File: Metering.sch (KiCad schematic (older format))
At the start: 18 parts, among them J1 Barrel_Jack_Switch, J10 Conn_01x15, J11 Conn_01x11, J2 Conn_01x15_Female, J3 Conn_01x15_Female, J4 Conn_01x15_Female, J5 Conn_01x15_Female, J6 Conn_01x15_Female, J7 Conn_01x15_Female, J8 Conn_01x15_Female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

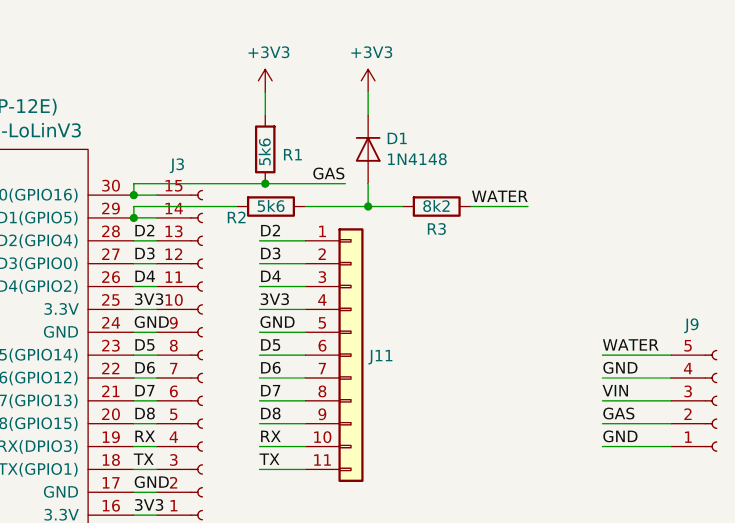
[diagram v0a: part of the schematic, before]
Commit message: add drills
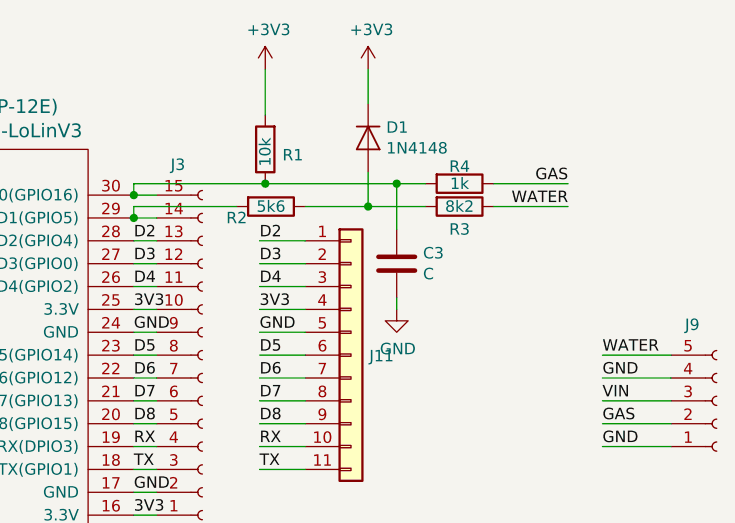
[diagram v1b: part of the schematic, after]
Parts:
- added C3: C, Capacitor_THT:C_Disc_D3.0mm_W2.0mm_P2.50mm, symbol Device:C
- added R4: 1k, w_pth_resistors:RC03, symbol Device:R
- R1: value 5k6 -> 10k
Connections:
- net GAS: now also R4.1; no longer J3.15 (Pin_15), R1.1, U1.30 (D0(GPIO16))
- net GND: now also C3.2
- new net: C3.1, J3.15 (Pin_15), R1.1, R4.2, U1.30 (D0(GPIO16))
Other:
- moved on the sheet: D1, R3
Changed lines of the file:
@@
 P 6875 3000
 F 0 "R1" H 6800 3025 50  0000 R CNN
-F 1 "5k6" V 6875 3075 50  0000 R CNN
+F 1 "10k" V 6875 3075 50  0000 R CNN
 F 2 "w_pth_resistors:RC03" V 6805 3000 50  0001 C CNN
 F 3 "~" H 6875 3000 50  0001 C CNN
@@
 L power:+3V3 #PWR0101
 U 1 1 5C44594E
-P 6875 2750
-F 0 "#PWR0101" H 6875 2600 50  0001 C CNN
-F 1 "+3V3" H 6890 2923 50  0000 C CNN
-F 2 "" H 6875 2750 50  0001 C CNN
-F 3 "" H 6875 2750 50  0001 C CNN
-	1    6875 2750
-	1    0    0    -1
-$EndComp
-Wire Wire Line
-	6875 2850 6875 2750
+P 6875 2650
+F 0 "#PWR0101" H 6875 2500 50  0001 C CNN
+F 1 "+3V3" H 6890 2823 50  0000 C CNN
+F 2 "" H 6875 2650 50  0001 C CNN
+F 3 "" H 6875 2650 50  0001 C CNN
+	1    6875 2650
+	1    0    0    -1
+$EndComp
+Wire Wire Line
+	6875 2850 6875 2650
 $Comp
 L Diode:1N4148 D1
 U 1 1 5C445B39
-P 7325 3000
-F 0 "D1" V 7279 3079 50  0000 L CNN
-F 1 "1N4148" V 7370 3079 50  0000 L CNN
-F 2 "Diode_THT:D_DO-35_SOD27_P7.62mm_Horizontal" H 7325 2825 50  0001 C CNN
-F 3 "http://www.nxp.com/documents/data_sheet/1N4148_1N4448.pdf" H 7325 3000 50  0001 C CNN
-	1    7325 3000
+P 7325 2950
+F 0 "D1" V 7279 3029 50  0000 L CNN
+F 1 "1N4148" V 7370 3029 50  0000 L CNN
+F 2 "Diode_THT:D_DO-35_SOD27_P7.62mm_Horizontal" H 7325 2775 50  0001 C CNN
+F 3 "http://www.nxp.com/documents/data_sheet/1N4148_1N4448.pdf" H 7325 2950 50  0001 C CNN
+	1    7325 2950
 	0    1    1    0
 $EndComp
@@
 	7050 3250 7325 3250
 Wire Wire Line
-	7325 3150 7325 3250
+	7325 3100 7325 3250
 $Comp
 L power:+3V3 #PWR0102
 U 1 1 5C445CAB
-P 7325 2750
-F 0 "#PWR0102" H 7325 2600 50  0001 C CNN
-F 1 "+3V3" H 7340 2923 50  0000 C CNN
-F 2 "" H 7325 2750 50  0001 C CNN
-F 3 "" H 7325 2750 50  0001 C CNN
-	1    7325 2750
-	1    0    0    -1
-$EndComp
-Wire Wire Line
-	7325 2750 7325 2850
-Wire Wire Line
-	6875 3150 7225 3150
-Text Label 7225 3150 2    50   ~ 0
+P 7325 2650
+F 0 "#PWR0102" H 7325 2500 50  0001 C CNN
+F 1 "+3V3" H 7340 2823 50  0000 C CNN
+F 2 "" H 7325 2650 50  0001 C CNN
+F 3 "" H 7325 2650 50  0001 C CNN
+	1    7325 2650
+	1    0    0    -1
+$EndComp
+Wire Wire Line
+	7325 2650 7325 2800
+Text Label 8200 3150 2    50   ~ 0
 GAS
-Text Label 8025 3250 2    50   ~ 0
+Text Label 8200 3250 2    50   ~ 0
 WATER
 $Comp
@@
 Wire Wire Line
 	4350 5525 4350 5600
-Wire Wire Line
-	8025 3250 7775 3250
 Connection ~ 7325 3250
 $Comp
 L Device:R R3
 U 1 1 5C65808C
-P 7625 3250
-F 0 "R3" V 7725 3250 50  0000 C CNN
-F 1 "8k2" V 7625 3250 50  0000 C CNN
-F 2 "w_pth_resistors:RC03" V 7555 3250 50  0001 C CNN
-F 3 "~" H 7625 3250 50  0001 C CNN
-	1    7625 3250
+P 7725 3250
+F 0 "R3" V 7825 3250 50  0000 C CNN
+F 1 "8k2" V 7725 3250 50  0000 C CNN
+F 2 "w_pth_resistors:RC03" V 7655 3250 50  0001 C CNN
+F 3 "~" H 7725 3250 50  0001 C CNN
+	1    7725 3250
 	0    1    1    0
 $EndComp
 Wire Wire Line
-	7475 3250 7325 3250
+	7575 3250 7325 3250
 $Comp
 L Connector:Conn_01x05_Female J9
@@
 Text Label 4475 5525 0    50   ~ 0
 3V3
+$Comp
+L Device:R R4
+U 1 1 5C5FE2F6
+P 7725 3150
+F 0 "R4" V 7650 3150 50  0000 C CNN
+F 1 "1k" V 7725 3150 50  0000 C CNN
+F 2 "w_pth_resistors:RC03" V 7655 3150 50  0001 C CNN
+F 3 "~" H 7725 3150 50  0001 C CNN
+	1    7725 3150
+	0    1    1    0
+$EndComp
+Wire Wire Line
+	6875 3150 7450 3150
+$Comp
+L Device:C C3
+U 1 1 5C6647B9
+P 7450 3500
+F 0 "C3" H 7565 3546 50  0000 L CNN
+F 1 "C" H 7565 3455 50  0000 L CNN
+F 2 "Capacitor_THT:C_Disc_D3.0mm_W2.0mm_P2.50mm" H 7488 3350 50  0001 C CNN
+F 3 "~" H 7450 3500 50  0001 C CNN
+	1    7450 3500
+	1    0    0    -1
+$EndComp
+Wire Wire Line
+	7875 3150 8200 3150
+Wire Wire Line
+	7875 3250 8200 3250
+Wire Wire Line
+	7450 3150 7450 3350
+Connection ~ 7450 3150
+Wire Wire Line
+	7450 3150 7575 3150
+$Comp
+L power:GND #PWR0112
+U 1 1 5C6B9E60
+P 7450 3700
+F 0 "#PWR0112" H 7450 3450 50  0001 C CNN
+F 1 "GND" H 7455 3527 50  0000 C CNN
+F 2 "" H 7450 3700 50  0001 C CNN
+F 3 "" H 7450 3700 50  0001 C CNN
+	1    7450 3700
+	1    0    0    -1
+$EndComp
+Wire Wire Line
+	7450 3650 7450 3700
 $EndSCHEMATC

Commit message: shorten board and use D2 instead of D0
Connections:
- net D2: now also C3.1, R1.1, R4.2
- new net: J3.15 (Pin_15), U1.30 (D0(GPIO16))
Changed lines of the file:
@@
 Wire Wire Line
 	6300 3300 6400 3300
-Connection ~ 6875 3150
 Wire Wire Line
 	6300 3700 6400 3700
@@
 D4
 Wire Wire Line
-	6300 3400 6400 3400
-Wire Wire Line
-	6300 3200 6300 3150
-Wire Wire Line
-	6300 3150 6875 3150
-Connection ~ 6300 3200
+	6300 3400 6350 3400
 Wire Wire Line
 	6300 3250 6750 3250
@@
 Wire Wire Line
 	7450 3650 7450 3700
+Wire Wire Line
+	6875 3150 6700 3150
+Connection ~ 6875 3150
+Wire Wire Line
+	6700 3150 6700 3375
+Wire Wire Line
+	6700 3375 6350 3375
+Wire Wire Line
+	6350 3375 6350 3400
+Connection ~ 6350 3400
+Wire Wire Line
+	6350 3400 6400 3400
 $EndSCHEMATC
